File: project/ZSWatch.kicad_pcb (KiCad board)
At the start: 4 copper layers, 41 x 38 mm, 74 parts, among them IC1 APDS-9306-065, IC10 FAN5622SX, IC11 XC9265A331MR-G, IC12 BMP581, IC13 BME688, IC14 LIS2MDLTR, IC15 DRV2603RUNT, IC2 ESDALC6V1W5, IC3 MAX1811ESA+, IC4 DMC2400UV-7, IC5 NCV300LSN36T1G, IC6 AT25SL128A, IC7 XC9265C181MR-G, IC8 BMI270, IC9 NTS0104GU12, M1 NORA-B106, X1 DOCK, X10 M-, X2 BATTERY, X3 GPIO0, X4 GPIO1, X5 GPIO2, X6 GPIO3, X7 GND, X8 GC9A01A_CST816S, X9 M+

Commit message: Initialize branch
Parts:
- removed the C1 at (149.1, 126.0)
- removed C10, C13, C15, C17, C19, C20, C21, C7, C8, C9: 100n, Capacitor_SMD:C_0603_1608Metric
- removed C11, C18, C4: 10u, Capacitor_SMD:C_0603_1608Metric
- removed C12: 1u, Capacitor_SMD:C_0603_1608Metric
- removed C14, C6: 22u, Capacitor_SMD:C_0603_1608Metric
- removed C16: 220n, Capacitor_SMD:C_0603_1608Metric
- removed C2: 4u7, Capacitor_SMD:C_0603_1608Metric
- removed C3: 2u2, Capacitor_SMD:C_0603_1608Metric
- removed G*** (x3): LOGO, LOGO
- removed the IC1 at (151.1, 126.0)
- removed IC10: FAN5622SX, Package_TO_SOT_SMD:TSOT-23-6
- removed IC11: XC9265A331MR-G, Package_SOT_SMD:SOT-25-5
- removed IC12: BMP581, Package_LGA_Kampi:Bosch_LGA-10_2x2mm_P0.5mm_ClockwisePinNumbering
- removed IC13: BME688, Package_LGA_Kampi:Bosch_LGA-8_3x3mm_P0.8mm_ClockwisePinNumbering
- removed IC14: LIS2MDLTR, Package_LGA_Kampi:LGA-12_2x2mm_P0.5mm
- removed IC15: DRV2603RUNT, Package_QFN:WQFN-10_2x2mm_P0.5mm
- removed IC2: ESDALC6V1W5, Package_SOT_SMD:SOT-325-5
- removed IC3: MAX1811ESA+, Package_SO:SOIC-8_3.9x4.9mm_P1.27mm
- removed IC4: DMC2400UV-7, Package_TO_SOT_SMD:SOT-563
- removed IC5: NCV300LSN36T1G, Package_SO:TSOP-5_1.65x3.05mm_P0.95mm
- removed IC7: XC9265C181MR-G, Package_SOT_SMD:SOT-25-5
- removed IC8: BMI270, Package_LGA_Kampi:LGA-14_3x2.5mm_P0.5mm_LayoutBorder3x4y
- removed IC9: NTS0104GU12, Package_QFN:XQFN-12-1.7x2mm_P0.4mm
- removed L1, L2: 10u, Inductor_SMD:L_0603_1608Metric
- removed the R1 at (164.1, 98.6)
- removed R11, R9: 100k, Resistor_SMD:R_0603_1608Metric
- removed R12: 10k, Resistor_SMD:R_0603_1608Metric
- removed the R2 at (168.4, 98.4)
- removed the R3 at (169.9, 99.4)
- removed R5: 1M, Resistor_SMD:R_0603_1608Metric
- removed R7, R8: 4k7, Resistor_SMD:R_0603_1608Metric
- removed S1, S2, S3, S4: TL6340AF160Q, E-Switch:TL6340AF160Q_Modified
- removed TP1: RESET, TestPoint:TestPoint_Pad_D1.0mm
- removed TP2: SCL, TestPoint:TestPoint_Pad_D1.0mm
- removed TP3: SDA, TestPoint:TestPoint_Pad_D1.0mm
- removed TP4: 3V3, TestPoint:TestPoint_Pad_D1.0mm
- removed TP5: BAT, TestPoint:TestPoint_Pad_D1.0mm
- removed TP6: 1V8, TestPoint:TestPoint_Pad_D1.0mm
- removed X10: M-, TestPoint:TestPoint_Pad_1.0x1.0mm
- removed the X2 at (160.7, 100.3)
- removed X3: GPIO0, TestPoint:TestPoint_Pad_1.0x1.0mm
- removed X4: GPIO1, TestPoint:TestPoint_Pad_1.0x1.0mm
- removed X5: GPIO2, TestPoint:TestPoint_Pad_1.0x1.0mm
- removed X6: GPIO3, TestPoint:TestPoint_Pad_1.0x1.0mm
- removed X7: GND, TestPoint:TestPoint_Pad_1.0x1.0mm
- removed X8: GC9A01A_CST816S, EastRising:ER-CON0.4-24P
- removed X9: M+, TestPoint:TestPoint_Pad_1.0x1.0mm
- added X1: Conn_01x02, Connector_PinHeader_2.54mm:PinHeader_1x02_P2.54mm_Vertical, F.Cu at (1.82, 1.82)
- renumbered C5 to C1, IC6 to IC1, R4 to R1, R6 to R2, R10 to R3, X1 to X2
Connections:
- M1 pad A2: DISPLAY_DC -> unconnected-(M1B-P0.12/TRACECLK-PadA2)
- M1 pad A3: TOUCH_SCL -> unconnected-(M1C-P1.03/I2C-PadA3)
- M1 pad A4: TOUCH_INT -> unconnected-(M1C-P1.00-PadA4)
- M1 pad A5: TOUCH_RST -> unconnected-(M1B-P0.20-PadA5)
- M1 pad B1: DISPLAY_CLK -> unconnected-(M1B-P0.08/TRACEDATA[3]-PadB1)
- M1 pad B3: DISPLAY_CS -> unconnected-(M1B-P0.11/TRACEDATA[0]-PadB3)
- M1 pad B4: TOUCH_SDA -> unconnected-(M1C-P1.02/I2C-PadB4)
- M1 pad B5: DISPLAY_RST -> unconnected-(M1B-P0.03/NFC2-PadB5)
- M1 pad C2: DISPLAY_DATA -> unconnected-(M1B-P0.09/TRACEDATA[2]-PadC2)
- M1 pad C8: GPIO0 -> unconnected-(M1B-P0.22-PadC8)
- M1 pad C9: unconnected-(M1A-D+-PadC9) -> MCU-D+
- M1 pad D1: DISPLAY_EN -> unconnected-(M1B-P0.15/QSPI[2]-PadD1)
- M1 pad D7: DISPLAY_BLK -> unconnected-(M1B-P0.23-PadD7)
- M1 pad D8: GPIO1 -> unconnected-(M1B-P0.04/AIN0-PadD8)
- M1 pad D9: unconnected-(M1A-D--PadD9) -> MCU_D-
- M1 pad E1: SENSOR_SCL -> unconnected-(M1B-P0.18/QSPI_CS-PadE1)
- M1 pad E2: INT2_LIS -> unconnected-(M1B-P0.14/QSPI[1]-PadE2)
- M1 pad E3: INT1_LIS -> unconnected-(M1B-P0.21-PadE3)
- M1 pad E8: GPIO2 -> unconnected-(M1B-P0.05/AIN1-PadE8)
- M1 pad E9: GPIO3 -> unconnected-(M1C-P1.05-PadE9)
- M1 pad F1: SENSOR_SDA -> unconnected-(M1B-P0.17/QSPI_CLK-PadF1)
- M1 pad F8: DRV_VIB_EN -> unconnected-(M1C-P1.14-PadF8)
- M1 pad F9: DRV_VIB_PWM -> unconnected-(M1C-P1.15-PadF9)
- M1 pad G1: BTN_4 -> unconnected-(M1C-P1.06-PadG1)
- M1 pad G3: BMP581_INT -> unconnected-(M1B-P0.25/AIN4-PadG3)
- M1 pad G8: BTN_3 -> unconnected-(M1C-P1.12-PadG8)
- M1 pad G9: CHG -> unconnected-(M1C-P1.13-PadG9)
- M1 pad H1: LIS2MDL_INT -> unconnected-(M1B-P0.24-PadH1)
- M1 pad H2: SWDIO -> MCU_SWDIO
- M1 pad H3: BTN_1 -> unconnected-(M1B-P0.27/AIN6-PadH3)
- M1 pad H8: BTN_2 -> unconnected-(M1B-P0.30-PadH8)
- M1 pad J2: SWDCLK -> MCU_SWDCLK
- M1 pad J7: BAT_MON_EN -> unconnected-(M1C-P1.10-PadJ7)
- M1 pad J8: BAT_MON -> unconnected-(M1B-P0.28/AIN7-PadJ8)
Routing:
- net GND: track 89.0 -> 27.1 mm, vias 55 -> 9
- net SENSOR_SCL: track 44.8 -> 0.00 mm, vias 10 -> 0
- net SENSOR_SDA: track 42.5 -> 0.00 mm, vias 3 -> 0
- net BTN_3: track 36.2 -> 0.00 mm, vias 2 -> 0
- net BTN_1: track 35.5 -> 0.00 mm, vias 2 -> 0
- net +1V8: track 42.5 -> 8.14 mm, vias 24 -> 5
- net DISPLAY_EN: track 34.1 -> 0.00 mm, vias 3 -> 0
- net +BATT: track 33.0 -> 0.00 mm, vias 4 -> 0
- net INT2_LIS: track 32.5 -> 0.00 mm, vias 2 -> 0
- net INT1_LIS: track 32.4 -> 0.00 mm, vias 2 -> 0
- net CHG: track 30.5 -> 0.00 mm, vias 2 -> 0
- net DRV_VIB_EN: track 26.6 -> 0.00 mm, vias 2 -> 0
- net DISPLAY_3V3: track 25.0 -> 0.00 mm, vias 3 -> 0
- net BMP581_INT: track 24.7 -> 0.00 mm, vias 2 -> 0
- net Net-(IC9-B4): track 24.7 -> 0.00 mm, vias 2 -> 0
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- removed copper zone on F.Cu, net +1V8
- removed copper zone on F.Cu, net +BATT
- removed copper zone on F.Cu, net DISPLAY_3V3
- removed copper zone on F.Cu, net GND
- removed copper zone on F.Cu, net Net-(IC11-LX)
- removed copper zone on F.Cu, net Net-(IC7-LX)
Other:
- outline, holes or cut-outs redrawn
- board text removed: "2.0.3"
- board text removed: "5V"
- board text removed: "Designed with"
- board text removed: "GND"
- board text removed: "Reset"
- board text removed: "x"
- board text removed: "y"

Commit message: Working on nPM1300 design
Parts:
- added C10: 10u, Capacitor_SMD:C_0603_1608Metric, F.Cu at (189.6, 102.1)
- added C11: 10u, Capacitor_SMD:C_0603_1608Metric, F.Cu at (198.0, 99.8)
- added C2: 100n, Capacitor_SMD:C_0603_1608Metric, F.Cu at (100.0, 101.2)
- added C3: 1u, Capacitor_SMD:C_0603_1608Metric, F.Cu at (199.5, 99.8)
- added C4: 2u2, Capacitor_SMD:C_0603_1608Metric, F.Cu at (206.5, 97.3)
- added C5: 1u, Capacitor_SMD:C_0603_1608Metric, F.Cu at (198.6, 97.5)
- added C6: 10u, Capacitor_SMD:C_0603_1608Metric, F.Cu at (190.2, 96.5)
- added C7: 10u, Capacitor_SMD:C_0603_1608Metric, F.Cu at (187.3, 103.1)
- added C8: 100n, Capacitor_SMD:C_0603_1608Metric, F.Cu at (192.9, 104.4)
- added C9: 10u, Capacitor_SMD:C_0603_1608Metric, F.Cu at (189.6, 99.0)
- added IC2: TS3USB221A, Package_QFN:UQFN-10_1.55x2.05mm_P0.5mm, F.Cu at (150.7, 111.9)
- added IC3: nPM1300-QEXX, Package_DFN_QFN:QFN-32-1EP_5x5mm_P0.5mm_EP3.6x3.6mm_ThermalVias, F.Cu at (193.9, 100.5)
- added L1: 2u2, Inductor_SMD_Kampi:L_0806_2016, F.Cu at (187.7, 98.7)
- added L2: 2u2, Inductor_SMD_Kampi:L_0806_2016, F.Cu at (187.3, 101.3)
- added R10: 1k8, Resistor_SMD:R_0603_1608Metric, F.Cu at (192.4, 127.0)
- added R12: 10k, Resistor_SMD:R_0603_1608Metric, F.Cu at (146.4, 108.7)
- added R4: 100k, Resistor_SMD:R_0603_1608Metric, F.Cu at (120.0, 96.5)
- added R7: 150k, Resistor_SMD:R_0603_1608Metric, F.Cu at (198.6, 102.2)
- added R9: 1k8, Resistor_SMD:R_0603_1608Metric, F.Cu at (189.4, 126.8)
- added X3: VBUS, Connector_PinHeader_2.54mm:PinHeader_1x02_P2.54mm_Vertical, F.Cu at (105.0, 95.1)
- added X4: VBAT, Molex:78171-0002, F.Cu at (212.4, 103.1)
- added X5: INT, Connector_PinHeader_2.54mm:PinHeader_1x02_P2.54mm_Vertical, F.Cu at (109.6, 95.1)
- X1: value Conn_01x02 -> VDISPLAY
- moved X1 135.6 mm to (100.3, 95.1)
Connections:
- M1 pad B9: unconnected-(M1A-VBUS-PadB9) -> Net-(IC3-VBUSOUT)
- M1 pad J3: RESETn -> MCU_RESETn
- X1 pad 1: +1V8 -> GND
- X1 pad 2: GND -> Net-(IC3-LSOUT1/VOUTLDO1)
- X2 pad 1: SWDCLK -> D+/SWDCLK
- X2 pad 2: SWDIO -> D-/SWDIO
- X2 pad 3: RESETn -> SEL_SWD
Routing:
- net SWDIO: track 24.0 -> 0.00 mm, vias 1 -> 0
- net SWDCLK: track 23.1 -> 0.00 mm, vias 1 -> 0
- net RESETn: track 22.8 -> 0.00 mm, vias 2 -> 0
- net MCU_SWDIO: track 0.00 -> 22.2 mm, vias 0 -> 1
- net MCU_RESETn: track 0.00 -> 19.6 mm, vias 0 -> 2
- net MCU_SWDCLK: track 0.00 -> 19.0 mm, vias 0 -> 1
- net unconnected-(M1B-P0.09/TRACEDATA[2]-PadC2): track 11.3 -> 0.00 mm, vias 1 -> 0
- net +1V8: track 8.14 -> 19.1 mm, vias 5 -> 6
- net Net-(IC3-SW2): track 0.00 -> 5.01 mm
- net Net-(IC3-SW1): track 0.00 -> 4.14 mm
- net VBUS: track 0.00 -> 3.63 mm
- net GND: track 27.1 -> 30.7 mm, vias 9 -> 16
- net Net-(IC3-VBUSOUT): track 0.00 -> 3.06 mm
- net +3V0: track 0.00 -> 2.38 mm
- net Net-(IC3-VSET1): track 0.00 -> 1.43 mm
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- added copper zone on F.Cu, net +1V8
- added copper zone on F.Cu, net +3V0
- added copper zone on F.Cu, net GND
- added copper zone on F.Cu, net Net-(IC3-VBAT)
- added copper zone on B.Cu, net VSYS
- added copper zone on F.Cu, net VSYS
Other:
- board size 41 x 38 mm -> 76 x 38.2 mm

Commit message: Working on nPM1300 design
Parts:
- removed R12: 10k, Resistor_SMD:R_0603_1608Metric
- added S2: TL6340AF160Q, E-Switch:TL6340AF160Q_Modified, F.Cu at (173.4, 102.9)
- added S3: TL6340AF160Q, E-Switch:TL6340AF160Q_Modified, F.Cu at (145.4, 102.9)
- moved C2 66.3 mm to (165.9, 108.6), turned to -90 degrees
- moved R7 49.8 mm to (152.9, 82.4), turned to 0 degrees
- moved C3 49.8 mm to (152.0, 84.7), turned to -90 degrees
- moved C11 46.9 mm to (153.5, 84.7), turned to -90 degrees
- moved C5 46.9 mm to (152.9, 87.0), turned to 180 degrees
- moved X4 46.1 mm to (166.5, 99.8), turned to 180 degrees
- moved C8 41.9 mm to (158.6, 80.2), turned to 0 degrees
- moved IC3 39.8 mm to (157.6, 84.1), turned to 180 degrees
- moved C10 33.9 mm to (161.9, 82.5), turned to 90 degrees
- moved C7 31.7 mm to (164.2, 81.4), turned to 180 degrees
- moved C9 30.8 mm to (161.9, 85.5), turned to -90 degrees
- moved C6 30.2 mm to (161.3, 88.0), turned to 0 degrees
- moved L2 29.4 mm to (164.2, 83.2), turned to 180 degrees
- moved L1 27.1 mm to (163.8, 85.9), turned to 90 degrees
- moved IC2 16.4 mm to (165.9, 105.5), turned to 180 degrees
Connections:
- IC2 pad 3: MCU_D+ -> MCU_D_P
- IC2 pad 4: MCU_D- -> MCU_D_N
- M1 pad C9: MCU-D+ -> MCU_D_N
- M1 pad D9: MCU_D- -> MCU_D_P
- M1 pad J3: MCU_RESETn -> unconnected-(M1A-~{RESET}-PadJ3)
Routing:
- net MCU_RESETn: track 19.6 -> 0.00 mm, vias 2 -> 0
- net SEL_SWD: track 0.00 -> 8.99 mm
- net D+/SWDCLK: track 0.00 -> 7.87 mm, vias 0 -> 1
- net D-/SWDIO: track 0.00 -> 7.86 mm, vias 0 -> 1
- net MCU_D_N: track 0.00 -> 7.01 mm
- net MCU_D_P: track 0.00 -> 6.95 mm
- net VSYS: track 0.17 -> 5.48 mm, vias 2 -> 3
- net MCU_SWDIO: track 22.2 -> 18.2 mm, vias 1 -> 2
- net GND: track 30.7 -> 33.4 mm, vias 16 -> 19
- net +3V0: track 2.38 -> 3.81 mm
- net MCU_SWDCLK: track 19.0 -> 19.4 mm, vias 1 -> 2
- removed copper zone on F.Cu, net Net-(IC3-VBAT)

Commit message: First design for PCBWay
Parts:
- removed S3: TL6340AF160Q, E-Switch:TL6340AF160Q_Modified
- added R8: 0R, Resistor_SMD:R_0805_2012Metric_Pad1.20x1.40mm_HandSolder, B.Cu at (156.8, 100.9)
- added S1: TL6340AF160Q, E-Switch:TL6340AF160Q_Modified, F.Cu at (145.4, 102.9)
- added TP1: 3V3, TestPoint:TestPoint_Pad_1.0x1.0mm, F.Cu at (143.8, 113.3)
- added TP2: 3V0, TestPoint:TestPoint_Pad_1.0x1.0mm, F.Cu at (143.8, 115.5)
- added TP3: 1V8, TestPoint:TestPoint_Pad_1.0x1.0mm, F.Cu at (143.8, 111.1)
- added TP4: GND, TestPoint:TestPoint_Pad_1.0x1.0mm, F.Cu at (143.8, 117.7)
- R4: value 100k -> 47k
- X5: renamed from X1; value VDISPLAY -> 3V3
- moved X5 57.9 mm to (152.1, 120.9), turned to 90 degrees
- moved C1 55.2 mm to (151.6, 102.6), turned to 180 degrees
- moved X4 49.8 mm to (152.1, 110.9), turned to 90 degrees
- moved R4 49.3 mm to (169.0, 101.6), turned to -90 degrees
- moved X2 47.4 mm to (152.1, 116.0), turned to 90 degrees
- moved C3 23.6 mm to (161.0, 103.6), turned to 180 degrees
- moved R3 23.5 mm to (166.7, 101.4), turned to 180 degrees
- moved R1 22.9 mm to (170.8, 119.3), turned to 180 degrees
- moved C6 22.7 mm to (155.4, 102.3), turned to 0 degrees
- moved C2 21.1 mm to (167.4, 99.2), turned to 90 degrees
- moved L1 19.5 mm to (155.4, 100.6), turned to 0 degrees
- moved C7 19.3 mm to (157.7, 101.3), turned to -90 degrees
- moved C9 19.0 mm to (165.9, 99.2), turned to 90 degrees
- moved C10 16.9 mm to (166.6, 96.9), turned to 0 degrees
- moved R2 16.9 mm to (174.2, 119.3), turned to 0 degrees
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- renumbered C4 to C1, C5 to C10, C1 to C11, C3 to C2, C8 to C3, C2 to C4, C9 to C5, C7 to C6, C10 to C7, C6 to C8, C11 to C9, IC3 to IC1, IC1 to IC3, L2 to L1, L1 to L2, R10 to R1, R9 to R2, R7 to R3, R1 to R5, R2 to R6, R3 to R7, X2 to X1, X5 to X2, X4 to X3, X3 to X4
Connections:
- C1 pad 1: Net-(IC3-VBAT) -> Net-(X3-Pin_1)
- IC1 pad 11: Net-(IC3-GPIO4) -> INT
- IC1 pad 15: GND -> BTN
- IC1 pad 16: Net-(IC3-VSET2) -> Net-(IC1-VSET2)
- IC1 pad 19: Net-(IC3-VBAT) -> Net-(IC1-VBAT)
- IC1 pad 29: Net-(IC3-LSOUT1/VOUTLDO1) -> Net-(IC1-LSOUT1/VOUTLDO1)
- M1 pad C9: MCU_D_N -> MCU_D_P
- M1 pad D9: MCU_D_P -> MCU_D_N
- M1 pad E1: unconnected-(M1B-P0.18/QSPI_CS-PadE1) -> SCL
- M1 pad F1: unconnected-(M1B-P0.17/QSPI_CLK-PadF1) -> SDA
- M1 pad H8: unconnected-(M1B-P0.30-PadH8) -> BTN
- M1 pad J9: unconnected-(M1B-P0.31-PadJ9) -> INT
- R4 pad 1: +3V0 -> GND
- R4 pad 2: SEL_SWD -> Net-(IC1-VSET2)
- X2 pad 1: Net-(IC3-GPIO4) -> INT
- X3 pad 1: Net-(IC3-VBAT) -> Net-(X3-Pin_1)
- X5 pad 1: GND -> Net-(IC1-LSOUT1/VOUTLDO1)
- X5 pad 2: Net-(IC3-LSOUT1/VOUTLDO1) -> GND
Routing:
- net INT: track 0.00 -> 52.8 mm, vias 0 -> 2
- net +3V0: track 3.81 -> 48.4 mm
- net Net-(IC1-LSOUT1/VOUTLDO1): track 0.00 -> 41.7 mm, vias 0 -> 2
- net BTN: track 0.00 -> 35.7 mm, vias 0 -> 3
- net SDA: track 0.00 -> 31.5 mm, vias 0 -> 2
- net SCL: track 0.00 -> 29.2 mm, vias 0 -> 2
- net VBUS: track 3.63 -> 26.1 mm, vias 0 -> 1
- net Net-(IC1-VBUSOUT): track 3.06 -> 16.5 mm, vias 0 -> 2
- net Net-(IC1-VBAT): track 0.00 -> 9.46 mm, vias 0 -> 1
- net Net-(X3-Pin_1): track 0.00 -> 5.53 mm, vias 0 -> 1
- net Net-(IC1-VSET2): track 0.00 -> 5.43 mm
- net GND: track 33.4 -> 35.9 mm, vias 19 -> 20
- net +1V8: track 19.1 -> 18.7 mm, vias 6 -> 11
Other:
- board size 76 x 38.2 mm -> 41 x 38 mm
- board text added: "+"
- board text added: "-"

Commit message: Add additional jumper for SEL pin
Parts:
- added X5: SEL, Connector_PinHeader_2.54mm:PinHeader_1x03_P2.54mm_Vertical, F.Cu at (157.2, 125.7)
- renumbered R3 to R1, R4 to R2, R1 to R3, R2 to R4, R8 to R5, R5 to R6, R6 to R7, R7 to R8, TP4 to TP1, TP1 to TP2, TP2 to TP3, TP3 to TP4, X5 to X6
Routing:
- net SEL_SWD: track 8.99 -> 29.9 mm
- net +3V0: track 48.4 -> 65.1 mm
- net INT: track 52.8 -> 57.0 mm
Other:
- board text added: "SWD"
- board text added: "USB"

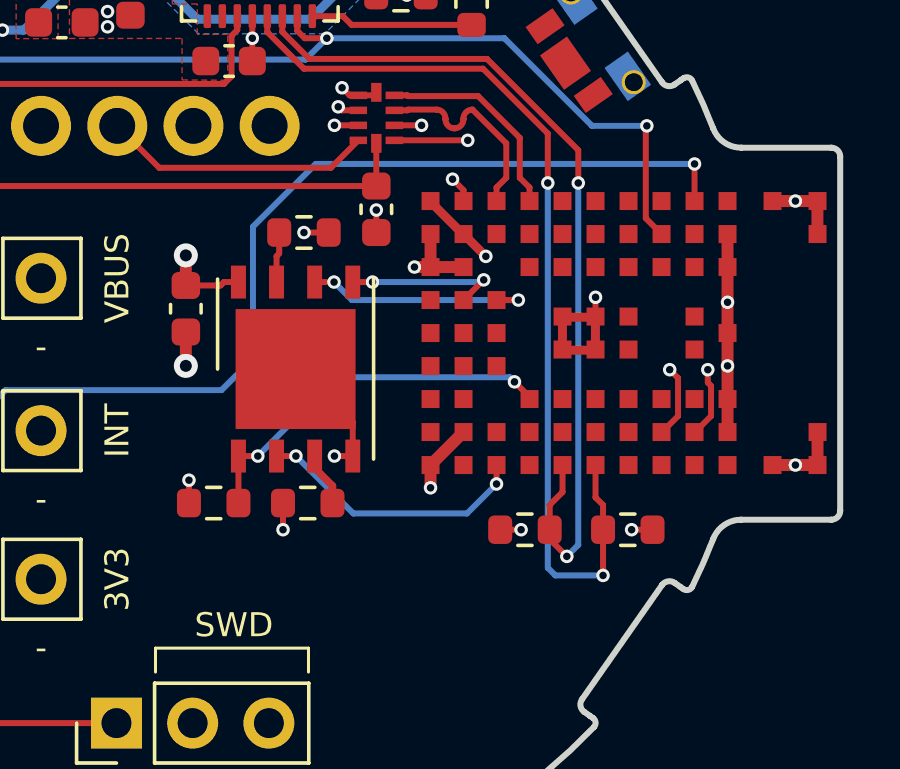
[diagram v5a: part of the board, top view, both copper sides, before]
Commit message: Add QSPI for flash
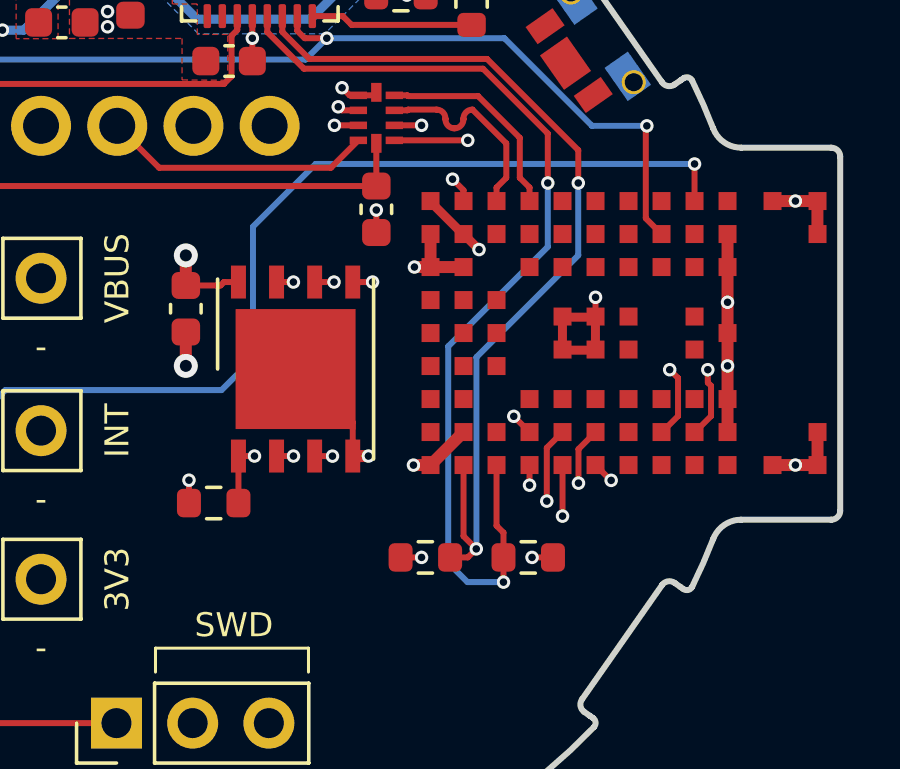
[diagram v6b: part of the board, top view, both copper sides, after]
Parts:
- removed R6, R8: 100k, Resistor_SMD:R_0603_1608Metric
- moved R3 3.44 mm to (167.5, 120.2)
- moved R4 3.44 mm to (170.9, 120.2)
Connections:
- IC3 pad 2: FLASH_SO -> FLASH_IO1
- IC3 pad 3: Net-(IC3-~{WP(I}/O2)) -> FLASH_IO2
- IC3 pad 5: FLASH_SI -> FLASH_IO0
- IC3 pad 7: Net-(IC3-~{HOLD(I}/O3)) -> FLASH_IO3
- M1 pad B1: unconnected-(M1B-P0.08/TRACEDATA[3]-PadB1) -> SCL
- M1 pad B6: FLASH_SI -> unconnected-(M1B-P0.01/XL2-PadB6)
- M1 pad C1: FLASH_SO -> SDA
- M1 pad C6: FLASH_CLK -> unconnected-(M1B-P0.00/XL1-PadC6)
- M1 pad D1: unconnected-(M1B-P0.15/QSPI[2]-PadD1) -> FLASH_IO2
- M1 pad D2: unconnected-(M1B-P0.13/QSPI[0]-PadD2) -> FLASH_IO0
- M1 pad D3: FLASH_CS -> unconnected-(M1B-P0.07/AIN3-PadD3)
- M1 pad E1: SCL -> FLASH_CS
- M1 pad E2: unconnected-(M1B-P0.14/QSPI[1]-PadE2) -> FLASH_IO1
- M1 pad F1: SDA -> FLASH_CLK
- M1 pad F2: unconnected-(M1B-P0.16/QSPI[3]-PadF2) -> FLASH_IO3
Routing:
- net FLASH_IO3: track 0.00 -> 15.8 mm, vias 0 -> 2
- net FLASH_IO1: track 0.00 -> 12.1 mm, vias 0 -> 2
- net FLASH_IO0: track 0.00 -> 9.85 mm, vias 0 -> 2
- net FLASH_SO: track 9.13 -> 0.00 mm, vias 2 -> 0
- net FLASH_IO2: track 0.00 -> 8.24 mm, vias 0 -> 2
- net FLASH_CLK: track 7.64 -> 14.8 mm
- net FLASH_SI: track 5.22 -> 0.00 mm, vias 2 -> 0
- net FLASH_CS: track 12.7 -> 14.9 mm
- net Net-(IC3-~{WP(I}/O2)): track 1.81 -> 0.00 mm
- net +1V8: track 18.7 -> 16.9 mm, vias 11 -> 9
- net Net-(IC3-~{HOLD(I}/O3)): track 1.69 -> 0.00 mm
- net SDA: track 31.5 -> 33.1 mm
- net SCL: track 29.2 -> 30.7 mm
- net GND: track 35.9 -> 35.3 mm
